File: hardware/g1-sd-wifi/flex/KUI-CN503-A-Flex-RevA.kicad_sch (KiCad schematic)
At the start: 2 parts, among them J1 CN503 row A solder contacts, J2 20-pin bottom-contact FPC tail

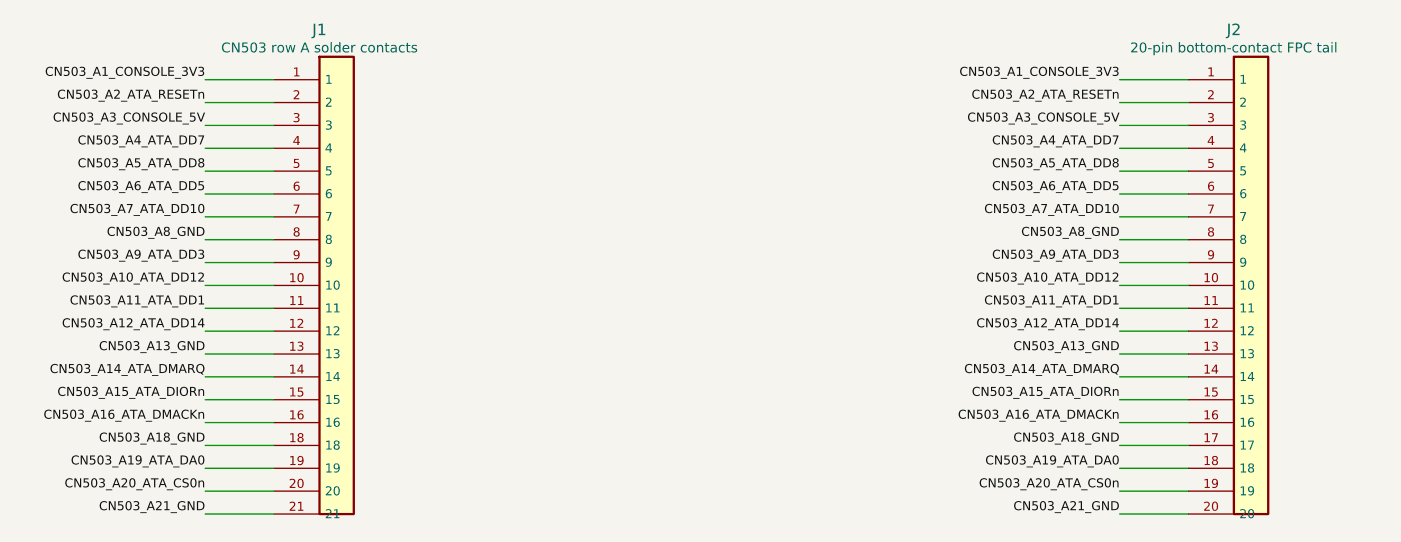
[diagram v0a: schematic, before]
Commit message: G1 safety: fuse the host 3.3-V entry; no console 5 V on the flex or carrier
Host 3.3 V reached about 30 carrier parts straight from two flex contacts,
and the two console-5-V contacts were joined by an unused carrier trace;
a short on either would load a console supply through 0.5 A connector
contacts with no fuse anywhere. Now:

- F21 (0467.500NR, 0.5 A fast, same 467 family as F20) sits between the one
  remaining 3.3-V entry, J51 B1, and CONSOLE_3V3. If it opens the buffers
  lose VCCB and isolate, and U25 reports the host rail absent.
- CN503 A1 (second 3.3 V) and A3/B3 (5 V) get no flex copper at all: no
  landing pad, no trace, only an unconnected mating finger, so a chafed
  flex cannot short a console supply. Their carrier socket pins are bare.
  flex-interface.json lists them; the flex and carrier generators and both
  checks read that list. Flex ERC/DRC/parity 0; carrier ERC 0, integration
  check pass (362 parts).
- The DSN export keeps the 5-V and storage supply nets on the 1 oz outer
  layers: on 0.5 oz inner copper a 0.25 mm track at the fuse current would
  overheat (IPC-2221).
- F21 is placed by the floorplan next to J51; board DRC 0, parity 0
  (unrouted).

Co-Authored-By: Claude Opus 5.5 <noreply@anthropic.com>
Claude-Session: https://claude.ai/code/session_01Gp9EYc2r9fMpZ7V8WtfonZ
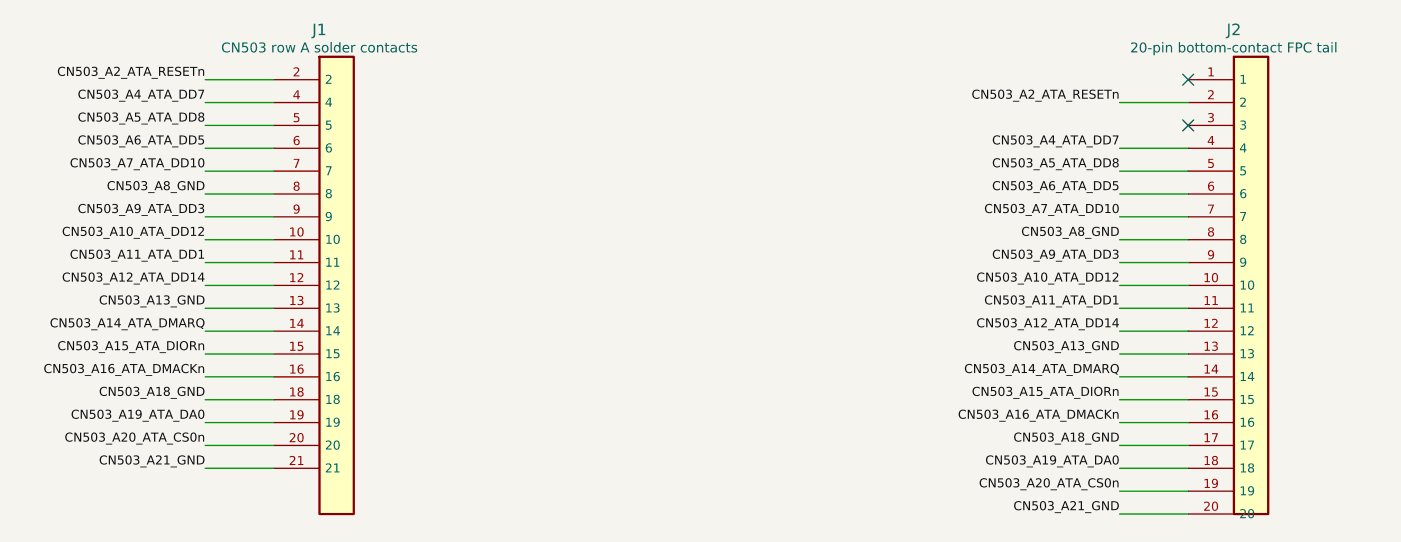
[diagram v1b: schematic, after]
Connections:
- net CN503_A1_CONSOLE_3V3: no longer names the net of J2.1
- net CN503_A1_CONSOLE_3V3: no longer J1.1
- net CN503_A3_CONSOLE_5V: no longer names the net of J2.3
- net CN503_A3_CONSOLE_5V: no longer J1.3
- no-connect marks 0 -> 2
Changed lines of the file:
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@@
 (wire (pts (xy 71.12 106.68) (xy 63.5 106.68)) (stroke (width 0) (type default)))
 (wire (pts (xy 71.12 109.22) (xy 63.5 109.22)) (stroke (width 0) (type default)))
-(wire (pts (xy 71.12 111.76) (xy 63.5 111.76)) (stroke (width 0) (type default)))
-(wire (pts (xy 71.12 114.3) (xy 63.5 114.3)) (stroke (width 0) (type default)))
-(wire (pts (xy 172.72 66.04) (xy 165.10000000000002 66.04)) (stroke (width 0) (type default)))
 (wire (pts (xy 172.72 68.58) (xy 165.10000000000002 68.58)) (stroke (width 0) (type default)))
-(wire (pts (xy 172.72 71.12) (xy 165.10000000000002 71.12)) (stroke (width 0) (type default)))
 (wire (pts (xy 172.72 73.66) (xy 165.10000000000002 73.66)) (stroke (width 0) (type default)))
 (wire (pts (xy 172.72 76.2) (xy 165.10000000000002 76.2)) (stroke (width 0) (type default)))
@@
 (wire (pts (xy 172.72 111.76) (xy 165.10000000000002 111.76)) (stroke (width 0) (type default)))
 (wire (pts (xy 172.72 114.3) (xy 165.10000000000002 114.3)) (stroke (width 0) (type default)))
-(label "CN503_A1_CONSOLE_3V3" (at 63.5 66.04 0) (effects (font (size 1 1)) (justify right bottom)))
-(label "CN503_A2_ATA_RESETn" (at 63.5 68.58 0) (effects (font (size 1 1)) (justify right bottom)))
-(label "CN503_A3_CONSOLE_5V" (at 63.5 71.12 0) (effects (font (size 1 1)) (justify right bottom)))
-(label "CN503_A4_ATA_DD7" (at 63.5 73.66 0) (effects (font (size 1 1)) (justify right bottom)))
-(label "CN503_A5_ATA_DD8" (at 63.5 76.2 0) (effects (font (size 1 1)) (justify right bottom)))
-(label "CN503_A6_ATA_DD5" (at 63.5 78.74 0) (effects (font (size 1 1)) (justify right bottom)))
-(label "CN503_A7_ATA_DD10" (at 63.5 81.28 0) (effects (font (size 1 1)) (justify right bottom)))
-(label "CN503_A8_GND" (at 63.5 83.82 0) (effects (font (size 1 1)) (justify right bottom)))
-(label "CN503_A9_ATA_DD3" (at 63.5 86.36 0) (effects (font (size 1 1)) (justify right bottom)))
-(label "CN503_A10_ATA_DD12" (at 63.5 88.9 0) (effects (font (size 1 1)) (justify right bottom)))
-(label "CN503_A11_ATA_DD1" (at 63.5 91.44 0) (effects (font (size 1 1)) (justify right bottom)))
-(label "CN503_A12_ATA_DD14" (at 63.5 93.98 0) (effects (font (size 1 1)) (justify right bottom)))
-(label "CN503_A13_GND" (at 63.5 96.52 0) (effects (font (size 1 1)) (justify right bottom)))
-(label "CN503_A14_ATA_DMARQ" (at 63.5 99.06 0) (effects (font (size 1 1)) (justify right bottom)))
-(label "CN503_A15_ATA_DIORn" (at 63.5 101.6 0) (effects (font (size 1 1)) (justify right bottom)))
-(label "CN503_A16_ATA_DMACKn" (at 63.5 104.14 0) (effects (font (size 1 1)) (justify right bottom)))
-(label "CN503_A18_GND" (at 63.5 106.68 0) (effects (font (size 1 1)) (justify right bottom)))
-(label "CN503_A19_ATA_DA0" (at 63.5 109.22 0) (effects (font (size 1 1)) (justify right bottom)))
-(label "CN503_A20_ATA_CS0n" (at 63.5 111.76 0) (effects (font (size 1 1)) (justify right bottom)))
-(label "CN503_A21_GND" (at 63.5 114.3 0) (effects (font (size 1 1)) (justify right bottom)))
-(label "CN503_A1_CONSOLE_3V3" (at 165.10000000000002 66.04 0) (effects (font (size 1 1)) (justify right bottom)))
+(label "CN503_A2_ATA_RESETn" (at 63.5 66.04 0) (effects (font (size 1 1)) (justify right bottom)))
+(label "CN503_A4_ATA_DD7" (at 63.5 68.58 0) (effects (font (size 1 1)) (justify right bottom)))
+(label "CN503_A5_ATA_DD8" (at 63.5 71.12 0) (effects (font (size 1 1)) (justify right bottom)))
+(label "CN503_A6_ATA_DD5" (at 63.5 73.66 0) (effects (font (size 1 1)) (justify right bottom)))
+(label "CN503_A7_ATA_DD10" (at 63.5 76.2 0) (effects (font (size 1 1)) (justify right bottom)))
+(label "CN503_A8_GND" (at 63.5 78.74 0) (effects (font (size 1 1)) (justify right bottom)))
+(label "CN503_A9_ATA_DD3" (at 63.5 81.28 0) (effects (font (size 1 1)) (justify right bottom)))
+(label "CN503_A10_ATA_DD12" (at 63.5 83.82 0) (effects (font (size 1 1)) (justify right bottom)))
+(label "CN503_A11_ATA_DD1" (at 63.5 86.36 0) (effects (font (size 1 1)) (justify right bottom)))
+(label "CN503_A12_ATA_DD14" (at 63.5 88.9 0) (effects (font (size 1 1)) (justify right bottom)))
+(label "CN503_A13_GND" (at 63.5 91.44 0) (effects (font (size 1 1)) (justify right bottom)))
+(label "CN503_A14_ATA_DMARQ" (at 63.5 93.98 0) (effects (font (size 1 1)) (justify right bottom)))
+(label "CN503_A15_ATA_DIORn" (at 63.5 96.52 0) (effects (font (size 1 1)) (justify right bottom)))
+(label "CN503_A16_ATA_DMACKn" (at 63.5 99.06 0) (effects (font (size 1 1)) (justify right bottom)))
+(label "CN503_A18_GND" (at 63.5 101.6 0) (effects (font (size 1 1)) (justify right bottom)))
+(label "CN503_A19_ATA_DA0" (at 63.5 104.14 0) (effects (font (size 1 1)) (justify right bottom)))
+(label "CN503_A20_ATA_CS0n" (at 63.5 106.68 0) (effects (font (size 1 1)) (justify right bottom)))
+(label "CN503_A21_GND" (at 63.5 109.22 0) (effects (font (size 1 1)) (justify right bottom)))
 (label "CN503_A2_ATA_RESETn" (at 165.10000000000002 68.58 0) (effects (font (size 1 1)) (justify right bottom)))
-(label "CN503_A3_CONSOLE_5V" (at 165.10000000000002 71.12 0) (effects (font (size 1 1)) (justify right bottom)))
 (label "CN503_A4_ATA_DD7" (at 165.10000000000002 73.66 0) (effects (font (size 1 1)) (justify right bottom)))
 (label "CN503_A5_ATA_DD8" (at 165.10000000000002 76.2 0) (effects (font (size 1 1)) (justify right bottom)))
@@
 (label "CN503_A20_ATA_CS0n" (at 165.10000000000002 111.76 0) (effects (font (size 1 1)) (justify right bottom)))
 (label "CN503_A21_GND" (at 165.10000000000002 114.3 0) (effects (font (size 1 1)) (justify right bottom)))
+(no_connect (at 172.72 66.04))
+(no_connect (at 172.72 71.12))
 (symbol (lib_id "KUI_Flex:CN503_A_Landing") (at 76.2 63.5 0) (unit 1) (in_bom no) (on_board yes) (dnp no)
 (property "Reference" "J1" (at 76.2 60.5 0) (effects (font (size 1.27 1.27))))
@@
 (property "Footprint" "KUI_Flex:CN503_A_20_SolderLanding_1.00mm" (at 76.2 63.5 0) (effects (font (size 1.27 1.27)) hide))
 (property "Datasheet" "" (at 0 0 0) (effects (font (size 1.27 1.27)) hide))
-(pin "1")
 (pin "2")
-(pin "3")
 (pin "4")
 (pin "5")
